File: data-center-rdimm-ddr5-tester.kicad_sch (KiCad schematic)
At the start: 2 parts

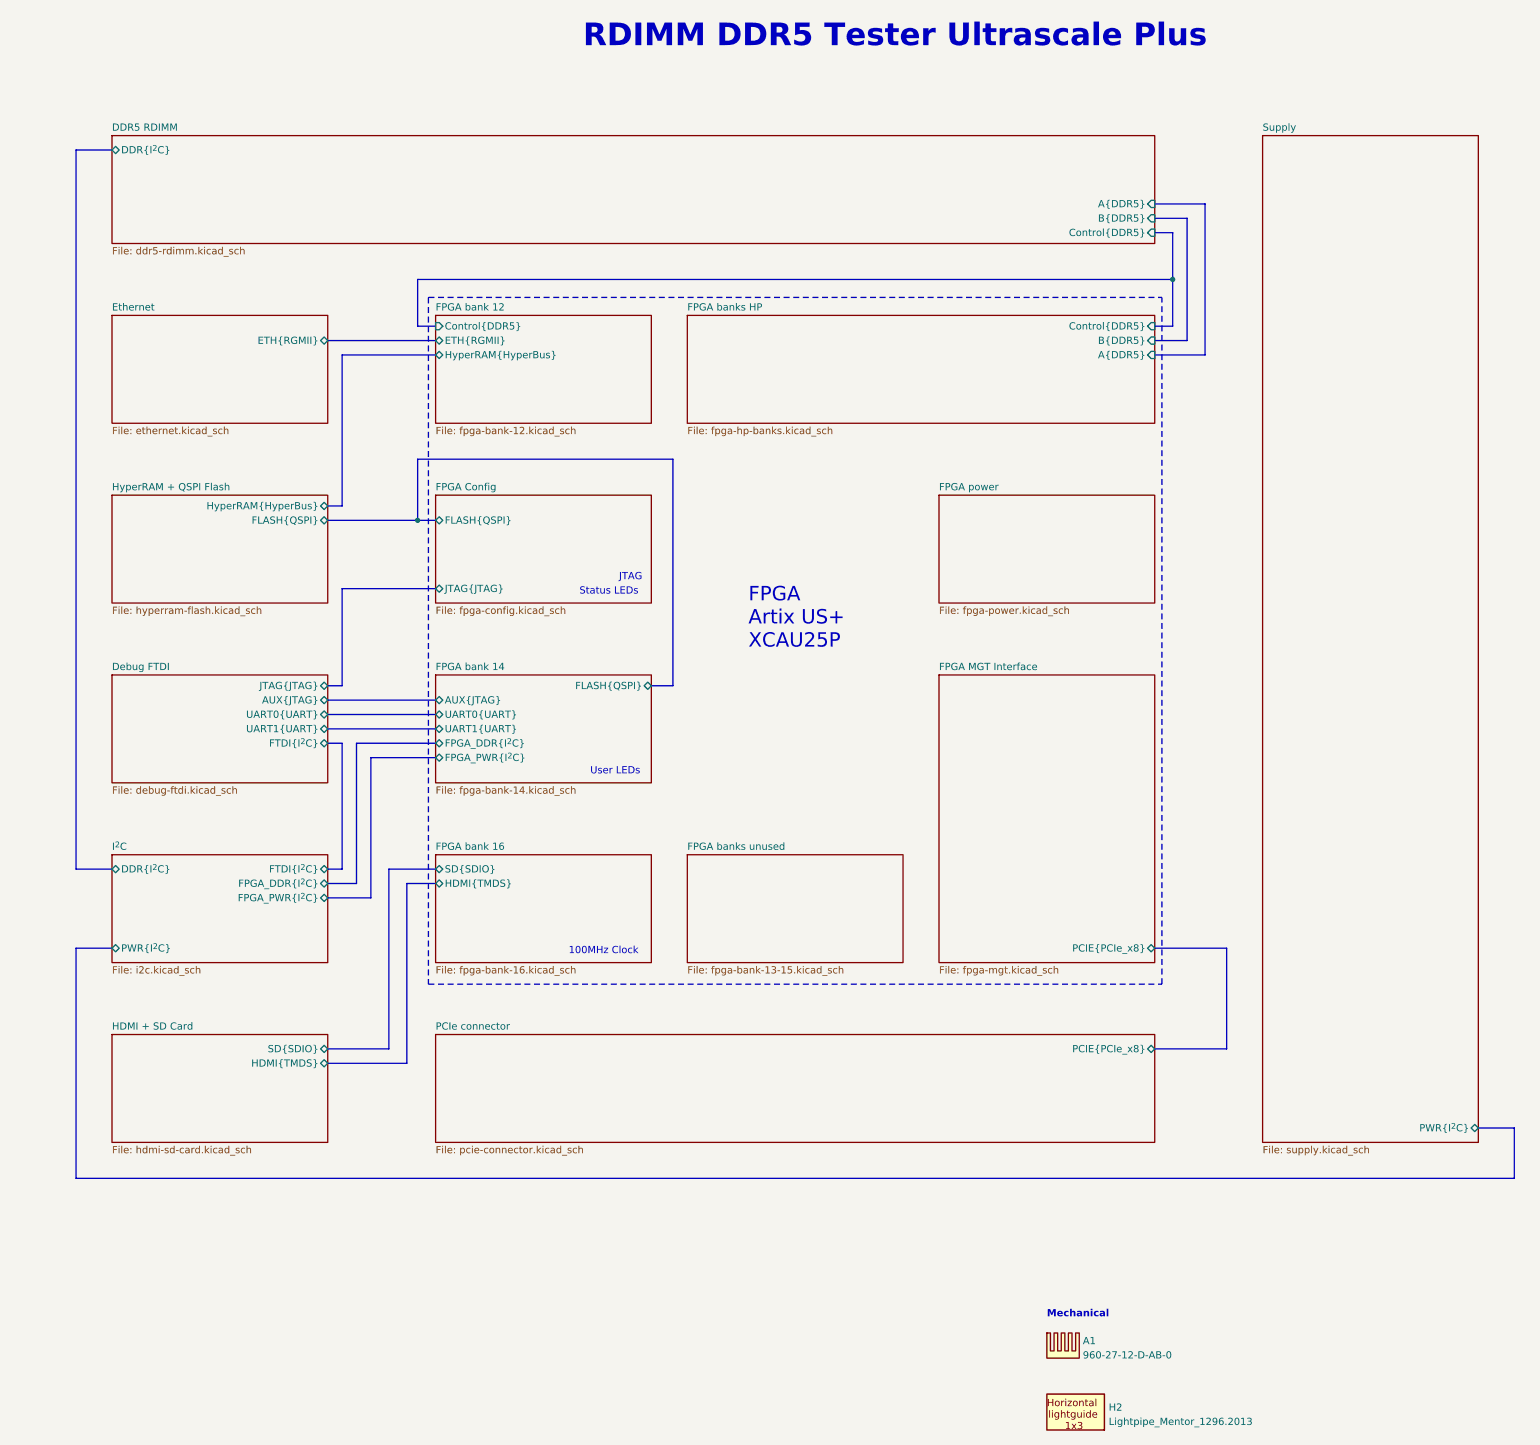
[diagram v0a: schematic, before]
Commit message: [#66521] Connect labels to DDR5 connector - define DDR5_RDIMM bus
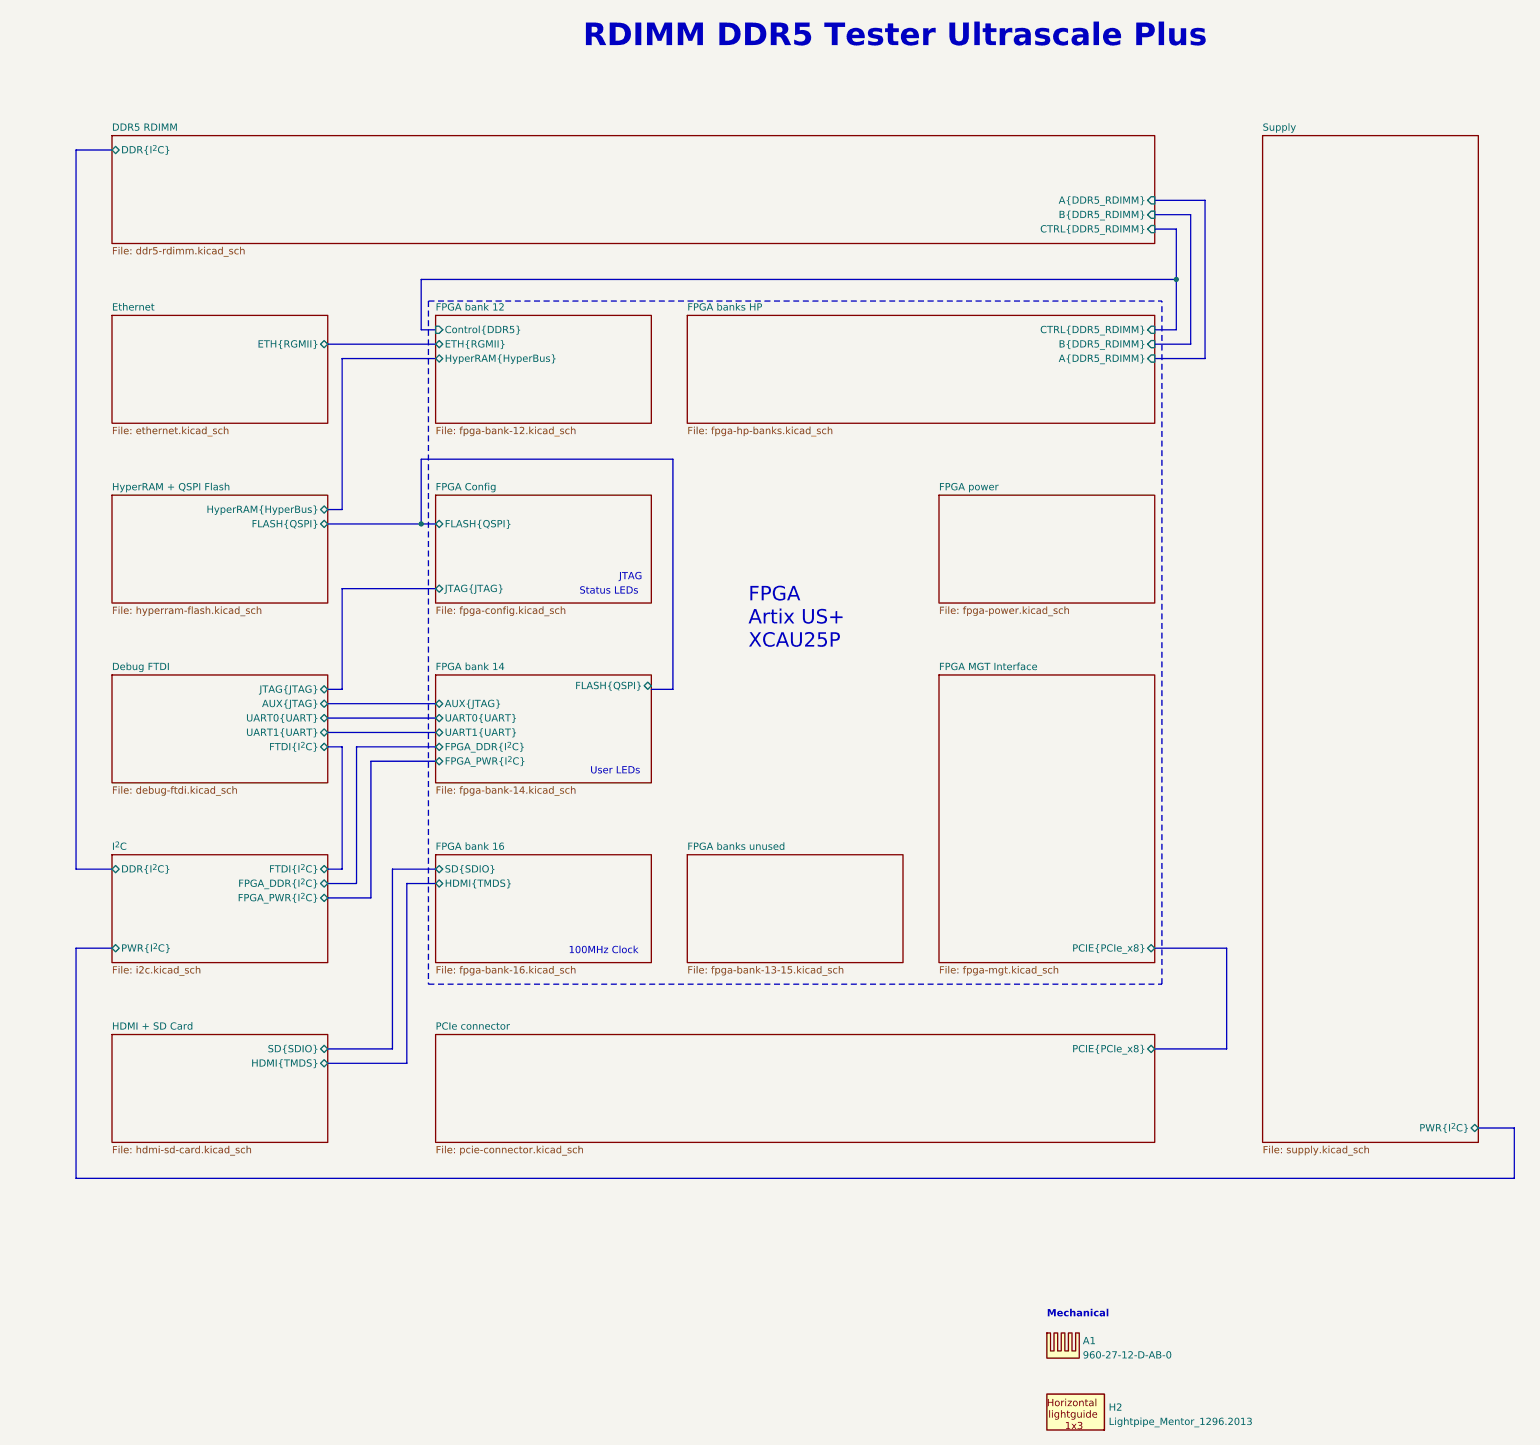
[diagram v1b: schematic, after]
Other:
- sheet DDR5 RDIMM ports: added A{DDR5_RDIMM}, B{DDR5_RDIMM}, CTRL{DDR5_RDIMM}; removed A{DDR5}, B{DDR5}, Control{DDR5}
- sheet FPGA banks HP ports: added A{DDR5_RDIMM}, B{DDR5_RDIMM}, CTRL{DDR5_RDIMM}; removed A{DDR5}, B{DDR5}, Control{DDR5}
